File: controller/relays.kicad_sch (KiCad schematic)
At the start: 34 parts, among them J10 Cooling #2, J11 Nutrient #2, J12 Heating #2, J5 Cooling #1, J6 Vent #1, J7 Nutrient #1, J8 Heating #1, J9 Vent #2, K1 G6DN-1ADC4.5, K11 G6DN-1ADC4.5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

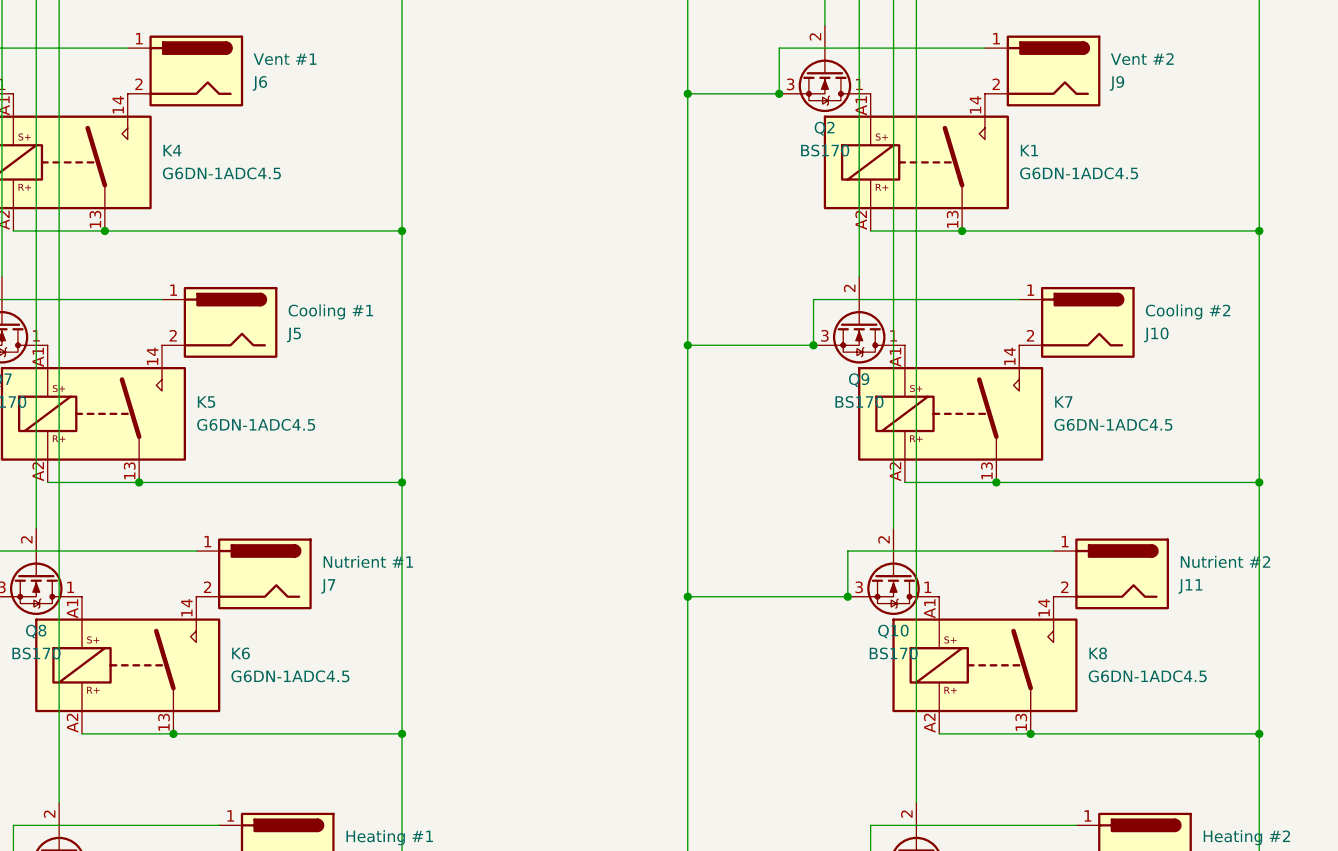
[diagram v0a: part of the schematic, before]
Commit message: updated relays and 250V part with actual circuit
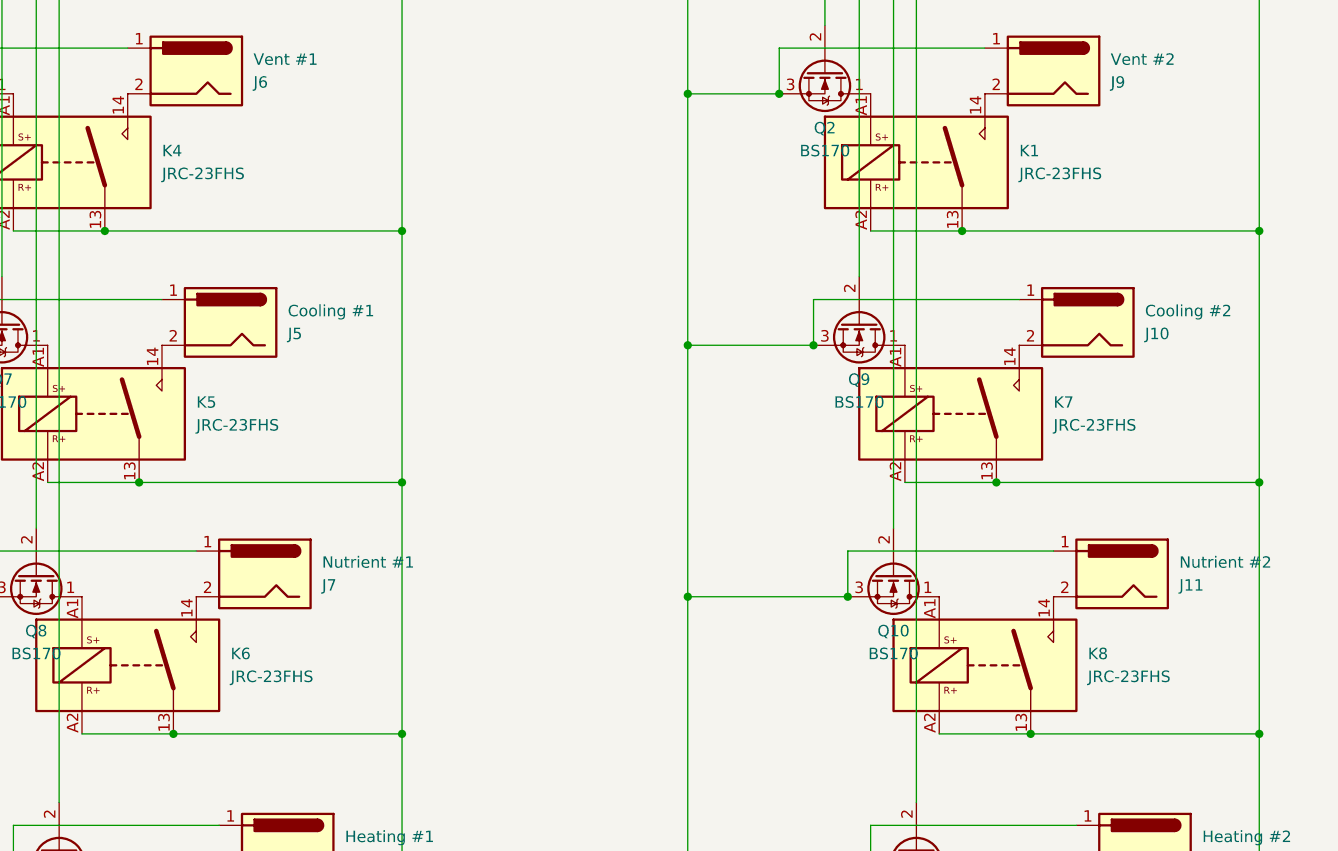
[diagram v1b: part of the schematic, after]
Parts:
- K1, K4, K5, K6, K7, K8: value G6DN-1ADC4.5 -> JRC-23FHS
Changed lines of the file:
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@@
 			)
 		)
-		(property "Value" "G6DN-1ADC4.5"
+		(property "Value" "JRC-23FHS"
 			(at 119.38 130.8099 0)
 			(effects
@@
 			)
 		)
-		(property "Value" "G6DN-1ADC4.5"
+		(property "Value" "JRC-23FHS"
 			(at 218.44 158.7499 0)
 			(effects
@@
 			)
 		)
-		(property "Value" "G6DN-1ADC4.5"
+		(property "Value" "JRC-23FHS"
 			(at 115.57 102.8699 0)
 			(effects
@@
 			)
 		)
-		(property "Value" "G6DN-1ADC4.5"
+		(property "Value" "JRC-23FHS"
 			(at 123.19 158.7499 0)
 			(effects
@@
 			)
 		)
-		(property "Value" "G6DN-1ADC4.5"
+		(property "Value" "JRC-23FHS"
 			(at 210.82 102.8699 0)
 			(effects
@@
 			)
 		)
-		(property "Value" "G6DN-1ADC4.5"
+		(property "Value" "JRC-23FHS"
 			(at 214.63 130.8099 0)
 			(effects
